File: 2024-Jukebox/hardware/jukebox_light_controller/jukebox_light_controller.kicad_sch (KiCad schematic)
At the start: 158 parts, among them J1 HEAD_LEDS, J10 BUTTON_3, J11 BUTTON_4, J12 BUTTON_5, J13 BUTTON_6, J14 BUTTON_7, J15 VOLUME, J16 DISPLAY_1, J17 DISPLAY_2, J2 MOUTH_LEDS, J3 76829-0004, J4 Conn_01x03, J5 ROTARY_SWITCH, J6 BUTTON_1, J7 USB_C_Receptacle_USB2.0, J8 BUTTON_2, J9 RJ45_Wuerth_7499010121A, Q1 2N7002, Q2 2N7002, SW1 SW_DIP_x03, SW2 SW_Push, SW3 SW_Push, U12 W25Q128JVS, U4 AMS1117-3.3, U5 RP2040, U6 W5500, Y1 12MHz, Y2 25MHz

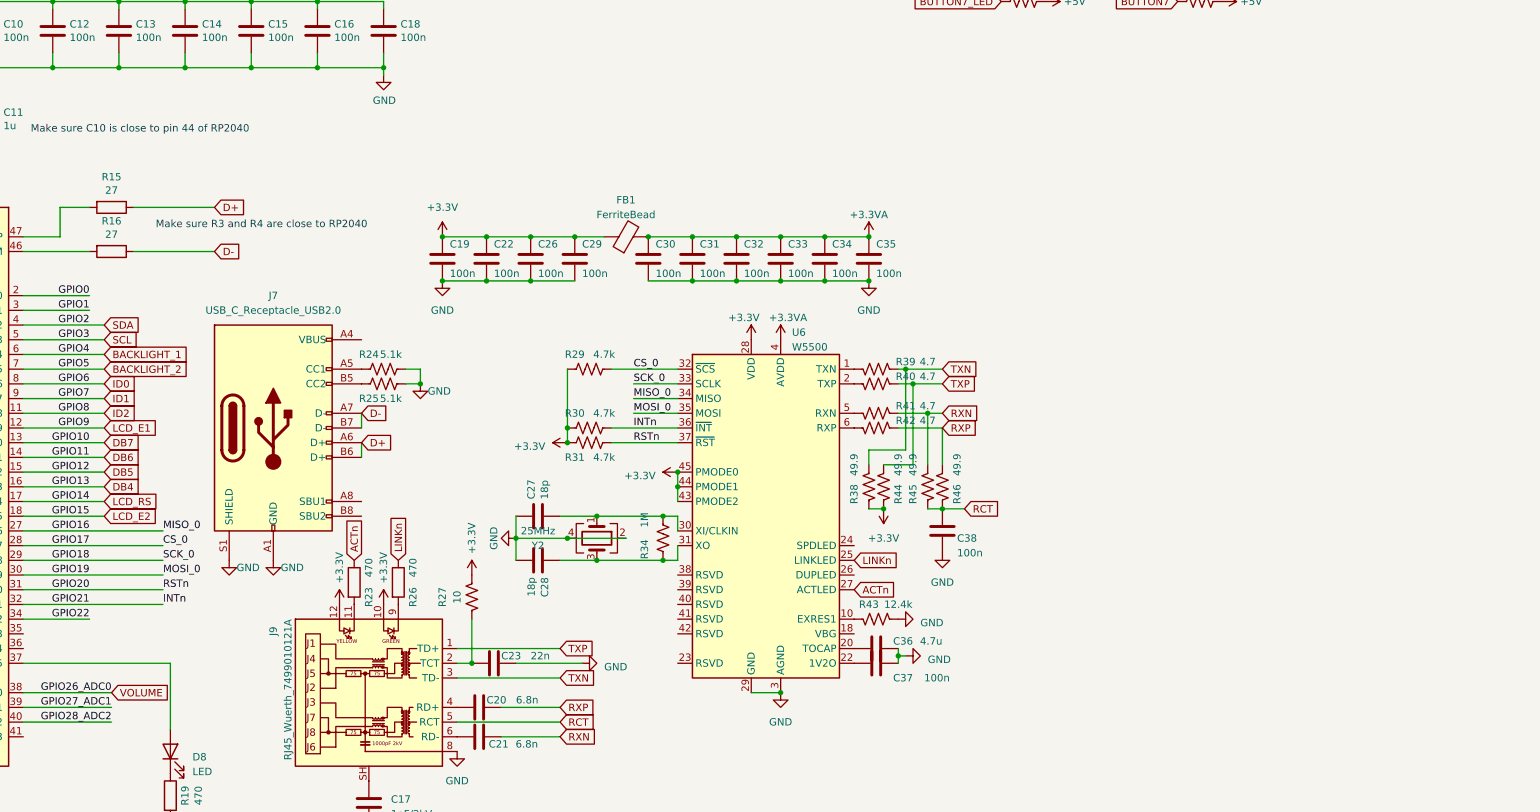
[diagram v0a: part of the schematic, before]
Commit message: Added level shifters to LCD display signals
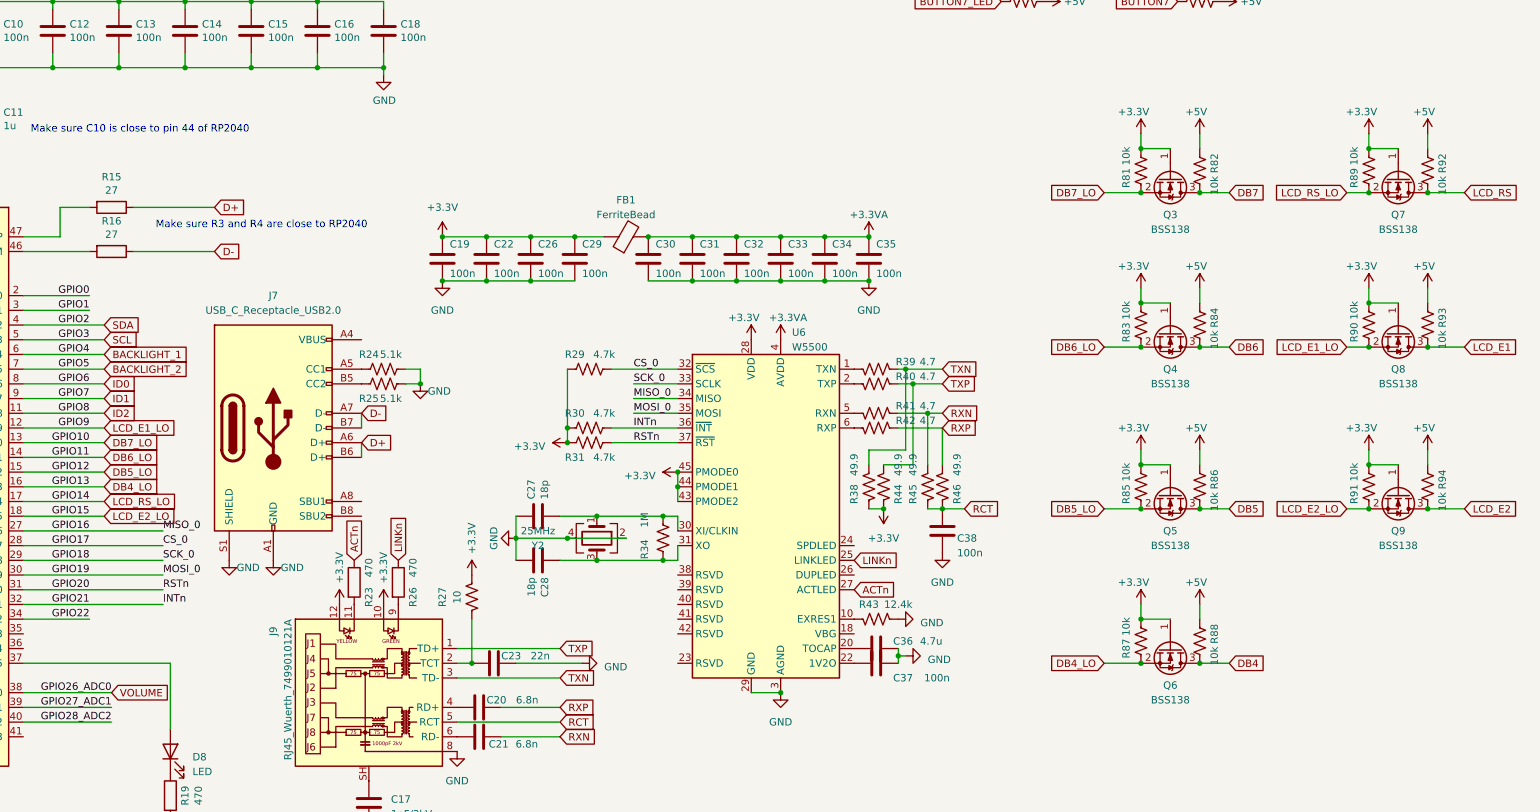
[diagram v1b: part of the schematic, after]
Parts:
- added Q3, Q4, Q5, Q6, Q7, Q8, Q9: BSS138, Package_TO_SOT_SMD:SOT-23, symbol Transistor_FET:BSS138
- added R81, R82, R83, R84, R85, R86, R87, R88, R89, R90, R91, R92, R93, R94: 10k, Resistor_SMD:R_0603_1608Metric, symbol Device:R_US
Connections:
- net +3.3V: now also Q3.1 (G), Q4.1 (G), Q5.1 (G), Q6.1 (G), Q7.1 (G), Q8.1 (G), Q9.1 (G), R81.2, R83.2, R85.2, R87.2, R89.2, R90.2, R91.2
- net +5V: now also R82.1, R84.1, R86.1, R88.1, R92.1, R93.1, R94.1
- net DB4: now also Q6.3 (D), R88.2; no longer U5.16 (GPIO13)
- net DB5: now also Q5.3 (D), R86.2; no longer U5.15 (GPIO12)
- net DB6: now also Q4.3 (D), R84.2; no longer U5.14 (GPIO11)
- net DB7: now also Q3.3 (D), R82.2; no longer U5.13 (GPIO10)
- net LCD_E1: now also Q8.3 (D), R93.2; no longer U5.12 (GPIO9)
- net LCD_E2: now also Q9.3 (D), R94.2; no longer U5.18 (GPIO15)
- net LCD_RS: now also Q7.3 (D), R92.2; no longer U5.17 (GPIO14)
- new net DB4_LO: Q6.2 (S), R87.1, U5.16 (GPIO13)
- new net DB5_LO: Q5.2 (S), R85.1, U5.15 (GPIO12)
- new net DB6_LO: Q4.2 (S), R83.1, U5.14 (GPIO11)
- new net DB7_LO: Q3.2 (S), R81.1, U5.13 (GPIO10)
- new net LCD_E1_LO: Q8.2 (S), R90.1, U5.12 (GPIO9)
- new net LCD_E2_LO: Q9.2 (S), R91.1, U5.18 (GPIO15)
- new net LCD_RS_LO: Q7.2 (S), R89.1, U5.17 (GPIO14)

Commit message: Updated schematic
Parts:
- removed Q1, Q2: 2N7002, Package_TO_SOT_SMD:SOT-23, symbol Transistor_FET:2N7002
- added Q1, Q10: MMBT2222, Package_TO_SOT_SMD:SOT-23, symbol Transistor_BJT:MMBT3904
- R79, R80: value 100 -> 470
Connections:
- net GND: now also Q1.2 (E), Q10.2 (E)
- net at J17.16 (Pin_16): now also Q10.3 (C)
- net at J16.16 (Pin_16): now also Q1.3 (C)
- net at R79.2: now also Q1.1 (B)
- net at R80.2: now also Q10.1 (B)
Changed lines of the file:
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@@
     )
   )
+  (symbol (lib_id "Transistor_BJT:MMBT3904") (at 162.56 88.9 0) (unit 1)
+    (in_bom yes) (on_board yes) (dnp no) (fields_autoplaced)
+    (property "Reference" "Q1" (at 167.64 87.63 0)
+      (effects (font (size 1.27 1.27)) (justify left))
+    )
+    (property "Value" "MMBT2222" (at 167.64 90.17 0)
+      (effects (font (size 1.27 1.27)) (justify left))
+    )
+    (property "Footprint" "Package_TO_SOT_SMD:SOT-23" (at 167.64 90.805 0)
+      (effects (font (size 1.27 1.27) italic) (justify left) hide)
+    )
+    (property "Datasheet" "https://www.onsemi.com/pdf/datasheet/pzt3904-d.pdf" (at 162.56 88.9 0)
+      (effects (font (size 1.27 1.27)) (justify left) hide)
+    )
+    (pin "1")
+    (pin "2")
+    (pin "3")
+    (instances
+      (project "jukebox_light_controller"
+        (path "/3d7cdb1e-a810-4ff2-a852-82c48438ee64"
+          (reference "Q1") (unit 1)
+        )
+      )
+    )
+  )
   (symbol (lib_id "power:GND") (at 264.16 31.75 90) (unit 1)
     (in_bom yes) (on_board yes) (dnp no) (fields_autoplaced)
@@
     )
   )
+  (symbol (lib_id "Transistor_BJT:MMBT3904") (at 205.74 90.17 0) (unit 1)
+    (in_bom yes) (on_board yes) (dnp no) (fields_autoplaced)
+    (property "Reference" "Q10" (at 210.82 88.9 0)
+      (effects (font (size 1.27 1.27)) (justify left))
+    )
+    (property "Value" "MMBT2222" (at 210.82 91.44 0)
+      (effects (font (size 1.27 1.27)) (justify left))
+    )
+    (property "Footprint" "Package_TO_SOT_SMD:SOT-23" (at 210.82 92.075 0)
+      (effects (font (size 1.27 1.27) italic) (justify left) hide)
+    )
+    (property "Datasheet" "https://www.onsemi.com/pdf/datasheet/pzt3904-d.pdf" (at 205.74 90.17 0)
+      (effects (font (size 1.27 1.27)) (justify left) hide)
+    )
+    (pin "1")
+    (pin "2")
+    (pin "3")
+    (instances
+      (project "jukebox_light_controller"
+        (path "/3d7cdb1e-a810-4ff2-a852-82c48438ee64"
+          (reference "Q10") (unit 1)
+        )
+      )
+    )
+  )
   (symbol (lib_id "Device:R_US") (at 373.38 182.88 180) (unit 1)
     (in_bom yes) (on_board yes) (dnp no)
@@
       (effects (font (size 1.27 1.27)))
     )
-    (property "Value" "100" (at 155.575 91.44 90)
+    (property "Value" "470" (at 155.575 91.44 90)
       (effects (font (size 1.27 1.27)))
     )
@@
       (effects (font (size 1.27 1.27)))
     )
-    (property "Value" "100" (at 198.755 92.71 90)
+    (property "Value" "470" (at 198.755 92.71 90)
       (effects (font (size 1.27 1.27)))
     )
@@
     )
   )
-  (symbol (lib_id "Transistor_FET:2N7002") (at 162.56 88.9 0) (unit 1)
-    (in_bom yes) (on_board yes) (dnp no)
-    (property "Reference" "Q1" (at 168.91 88.265 0)
-      (effects (font (size 1.27 1.27)) (justify left))
-    )
-    (property "Value" "2N7002" (at 168.91 90.805 0)
-      (effects (font (size 1.27 1.27)) (justify left))
-    )
-    (property "Footprint" "Package_TO_SOT_SMD:SOT-23" (at 167.64 90.805 0)
-      (effects (font (size 1.27 1.27) italic) (justify left) hide)
-    )
-    (property "Datasheet" "https://www.onsemi.com/pub/Collateral/NDS7002A-D.PDF" (at 162.56 88.9 0)
-      (effects (font (size 1.27 1.27)) (justify left) hide)
-    )
-    (pin "1")
-    (pin "2")
-    (pin "3")
-    (instances
-      (project "jukebox_light_controller"
-        (path "/3d7cdb1e-a810-4ff2-a852-82c48438ee64"
-          (reference "Q1") (unit 1)
-        )
-      )
-    )
-  )
   (symbol (lib_id "Device:R") (at 156.21 142.24 270) (unit 1)
     (in_bom yes) (on_board yes) (dnp no)
@@
         )
       )
-    )
-  )
-  (symbol (lib_id "Transistor_FET:2N7002") (at 205.74 90.17 0) (unit 1)
-    (in_bom yes) (on_board yes) (dnp no)
-    (property "Reference" "Q2" (at 212.09 89.535 0)
-      (effects (font (size 1.27 1.27)) (justify left))
-    )
-    (property "Value" "2N7002" (at 212.09 92.075 0)
-      (effects (font (size 1.27 1.27)) (justify left))
-    )
-    (property "Footprint" "Package_TO_SOT_SMD:SOT-23" (at 210.82 92.075 0)
-      (effects (font (size 1.27 1.27) italic) (justify left) hide)
-    )
-    (property "Datasheet" "https://www.onsemi.com/pub/Collateral/NDS7002A-D.PDF" (at 205.74 90.17 0)
-      (effects (font (size 1.27 1.27)) (justify left) hide)
-    )
-    (pin "1")
-    (pin "2")
-    (pin "3")
-    (instances
-      (project "jukebox_light_controller"
-        (path "/3d7cdb1e-a810-4ff2-a852-82c48438ee64"
-          (reference "Q2") (unit 1)
-        )
-      )

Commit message: Minor fixes
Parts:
- R53, R55, R56, R57, R58, R59: value 5.1k -> 1k
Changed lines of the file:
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@@
       (effects (font (size 1.27 1.27)))
     )
-    (property "Value" "5.1k" (at 316.23 81.28 90)
+    (property "Value" "1k" (at 316.23 81.28 90)
       (effects (font (size 1.27 1.27)))
     )
@@
       (effects (font (size 1.27 1.27)))
     )
-    (property "Value" "5.1k" (at 316.23 86.36 90)
+    (property "Value" "1k" (at 316.23 86.36 90)
       (effects (font (size 1.27 1.27)))
     )
@@
       (effects (font (size 1.27 1.27)))
     )
-    (property "Value" "5.1k" (at 316.23 91.44 90)
+    (property "Value" "1k" (at 316.23 91.44 90)
       (effects (font (size 1.27 1.27)))
     )
@@
       (effects (font (size 1.27 1.27)))
     )
-    (property "Value" "5.1k" (at 316.23 93.98 90)
+    (property "Value" "1k" (at 316.23 93.98 90)
       (effects (font (size 1.27 1.27)))
     )
@@
       (effects (font (size 1.27 1.27)))
     )
-    (property "Value" "5.1k" (at 316.23 96.52 90)
+    (property "Value" "1k" (at 316.23 96.52 90)
       (effects (font (size 1.27 1.27)))
     )
@@
       (effects (font (size 1.27 1.27)))
     )
-    (property "Value" "5.1k" (at 316.23 88.9 90)
+    (property "Value" "1k" (at 316.23 88.9 90)
       (effects (font (size 1.27 1.27)))
     )

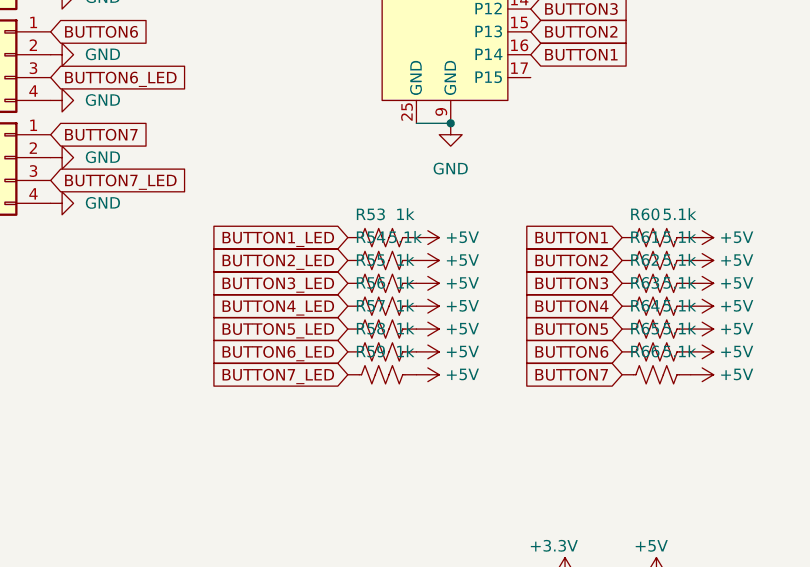
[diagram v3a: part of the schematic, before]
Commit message: Updated pullup resistor values
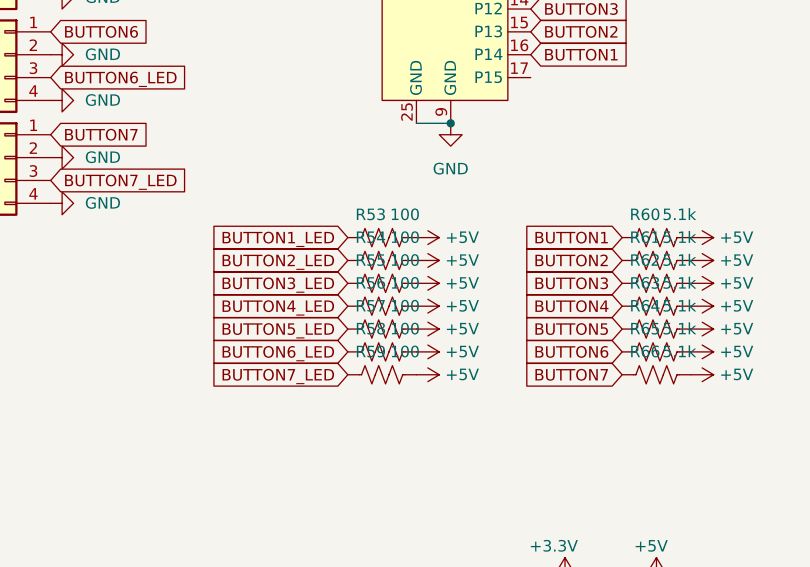
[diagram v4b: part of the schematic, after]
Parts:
- R53, R55, R56, R57, R58, R59: value 1k -> 100
- R54: value 5.1k -> 100
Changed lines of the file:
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@@
       (effects (font (size 1.27 1.27)))
     )
-    (property "Value" "5.1k" (at 316.23 83.82 90)
+    (property "Value" "100" (at 316.23 83.82 90)
       (effects (font (size 1.27 1.27)))
     )
@@
       (effects (font (size 1.27 1.27)))
     )
-    (property "Value" "1k" (at 316.23 81.28 90)
+    (property "Value" "100" (at 316.23 81.28 90)
       (effects (font (size 1.27 1.27)))
     )
@@
       (effects (font (size 1.27 1.27)))
     )
-    (property "Value" "1k" (at 316.23 86.36 90)
+    (property "Value" "100" (at 316.23 86.36 90)
       (effects (font (size 1.27 1.27)))
     )
@@
       (effects (font (size 1.27 1.27)))
     )
-    (property "Value" "1k" (at 316.23 91.44 90)
+    (property "Value" "100" (at 316.23 91.44 90)
       (effects (font (size 1.27 1.27)))
     )
@@
       (effects (font (size 1.27 1.27)))
     )
-    (property "Value" "1k" (at 316.23 93.98 90)
+    (property "Value" "100" (at 316.23 93.98 90)
       (effects (font (size 1.27 1.27)))
     )
@@
       (effects (font (size 1.27 1.27)))
     )
-    (property "Value" "1k" (at 316.23 96.52 90)
+    (property "Value" "100" (at 316.23 96.52 90)
       (effects (font (size 1.27 1.27)))
     )
@@
       (effects (font (size 1.27 1.27)))
     )
-    (property "Value" "1k" (at 316.23 88.9 90)
+    (property "Value" "100" (at 316.23 88.9 90)
       (effects (font (size 1.27 1.27)))
     )

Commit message: Update jukebox_light_controller.kicad_sch
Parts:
- R53, R54, R55, R56, R57, R58: value 100 -> 1k
- Rv: renamed from R59; value 100 -> 1k
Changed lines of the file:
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@@
       (effects (font (size 1.27 1.27)))
     )
-    (property "Value" "100" (at 316.23 83.82 90)
+    (property "Value" "1k" (at 316.23 83.82 90)
       (effects (font (size 1.27 1.27)))
     )
@@
       (effects (font (size 1.27 1.27)))
     )
-    (property "Value" "100" (at 316.23 81.28 90)
+    (property "Value" "1k" (at 316.23 81.28 90)
       (effects (font (size 1.27 1.27)))
     )
@@
       (effects (font (size 1.27 1.27)))
     )
-    (property "Value" "100" (at 316.23 86.36 90)
+    (property "Value" "1k" (at 316.23 86.36 90)
       (effects (font (size 1.27 1.27)))
     )
@@
       (effects (font (size 1.27 1.27)))
     )
-    (property "Value" "100" (at 316.23 91.44 90)
+    (property "Value" "1k" (at 316.23 91.44 90)
       (effects (font (size 1.27 1.27)))
     )
@@
       (effects (font (size 1.27 1.27)))
     )
-    (property "Value" "100" (at 316.23 93.98 90)
+    (property "Value" "1k" (at 316.23 93.98 90)
       (effects (font (size 1.27 1.27)))
     )
@@
   (symbol (lib_id "Device:R_US") (at 313.69 99.06 90) (unit 1)
     (in_bom yes) (on_board yes) (dnp no)
-    (property "Reference" "R59" (at 312.42 96.52 90)
+    (property "Reference" "Rv" (at 312.42 96.52 90)
       (effects (font (size 1.27 1.27)))
     )
-    (property "Value" "100" (at 316.23 96.52 90)
+    (property "Value" "1k" (at 316.23 96.52 90)
       (effects (font (size 1.27 1.27)))
     )
@@
       (project "jukebox_light_controller"
         (path "/3d7cdb1e-a810-4ff2-a852-82c48438ee64"
-          (reference "R59") (unit 1)
+          (reference "Rv") (unit 1)
         )
       )
@@
       (effects (font (size 1.27 1.27)))
     )
-    (property "Value" "100" (at 316.23 88.9 90)
+    (property "Value" "1k" (at 316.23 88.9 90)
       (effects (font (size 1.27 1.27)))
     )
